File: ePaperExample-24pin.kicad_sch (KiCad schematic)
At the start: 21 parts, among them J1 Conn_01x24_MountingPin, Q1 Q_NMOS_GSD

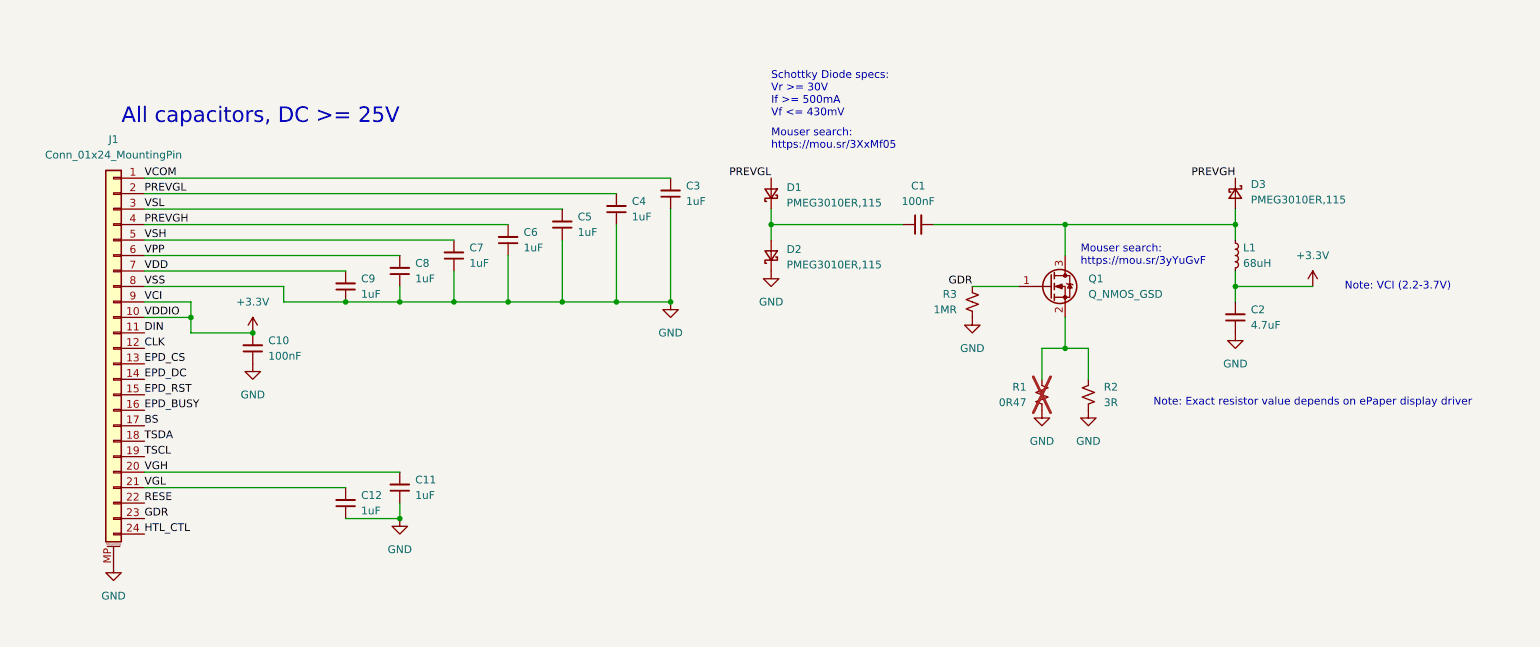
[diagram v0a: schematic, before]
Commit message: Updated to reflect tested board
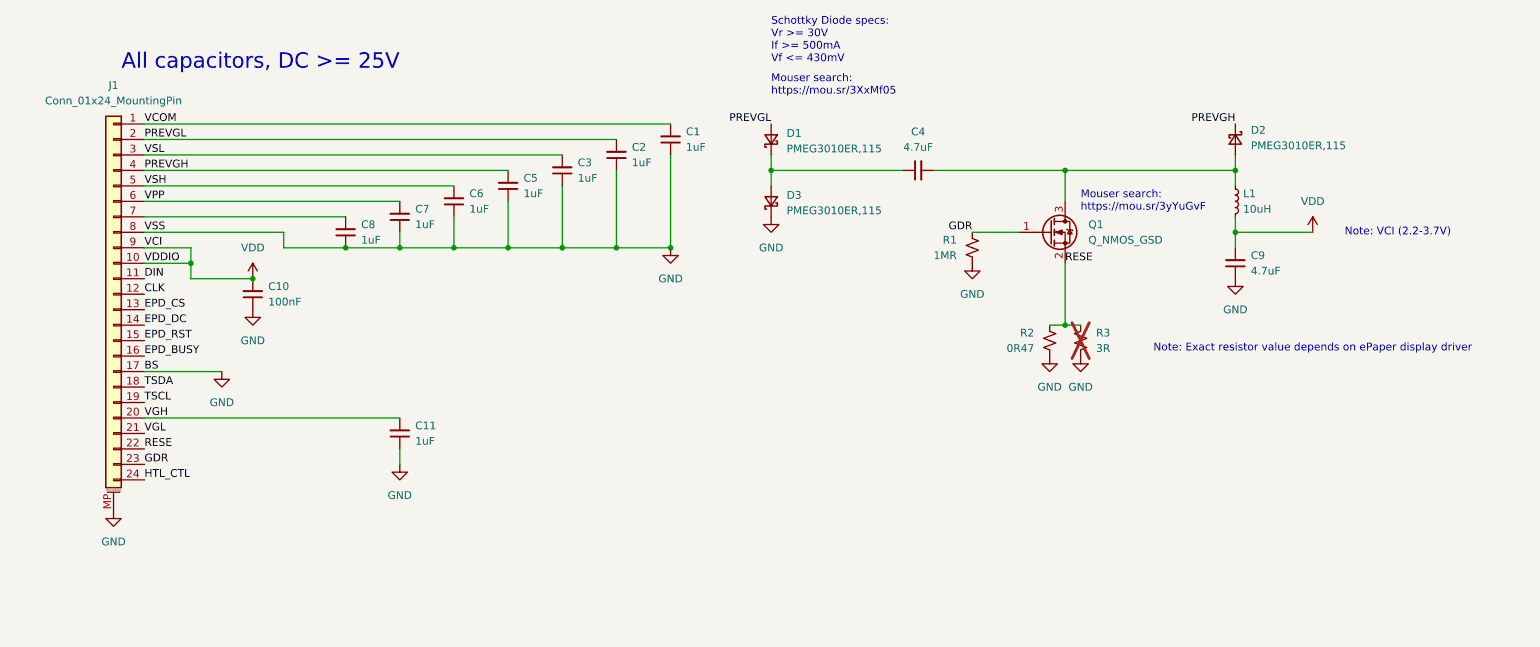
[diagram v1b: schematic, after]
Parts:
- removed C12: 1uF, Capacitor_SMD:C_0402_1005Metric, symbol Device:C_Small
- C1: value 100nF -> 1uF; LCSC (none) -> C52923
- C10: LCSC (none) -> C307331
- C11, C3, C5, C6, C7, C8: LCSC (none) -> C52923
- C2: value 4.7uF -> 1uF; LCSC (none) -> C52923
- C4, C9: value 1uF -> 4.7uF; LCSC (none) -> C2858031
- D1, D2, D3: LCSC (none) -> C456106
- J1: LCSC (none) -> C2911766
- L1: value 68uH -> 10uH; footprint Inductor_SMD:L_Bourns-SRN6028 -> Inductor_SMD:L_0805_2012Metric; LCSC (none) -> C2909263; MPN NR6028T680M -> (none)
- Q1: LCSC (none) -> C414015
- R1: value 0R47 -> 1MR; footprint (none) -> Resistor_SMD:R_0402_1005Metric; LCSC (none) -> C26083; now fitted; now in the parts list
- R2: value 3R -> 0R47; LCSC (none) -> C186564
- R3: value 1MR -> 3R; footprint Resistor_SMD:R_0402_1005Metric -> Resistor_SMD:R_0603_1608Metric; LCSC (none) -> C23157; now not fitted
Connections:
- net BS is gone; now on net GND: J1.17 (Pin_17)
- net GDR: now also R1.1; no longer R3.1
- net GND: now also C1.1, D3.1 (K); no longer C4.1, D2.1 (K)
- net PREVGH: now also C5.2, D2.1 (K); no longer C6.2, D3.1 (K)
- net PREVGL: now also C2.2; no longer C4.2
- net RESE: now also Q1.2 (S), R2.1, R3.1
- net VCOM: now also C1.2; no longer C3.2
- net VDD: now also C10.2, J1.10 (Pin_10), J1.9 (Pin_9), L1.2; no longer J1.7 (Pin_7)
- net VPP: now also C7.2; no longer C8.2
- net VSH: now also C6.2; no longer C7.2
- net VSL: now also C3.2; no longer C5.2
- net at L1.1, Q1.3 (D): now also C4.2, D2.2 (A); no longer C1.2, D3.2 (A)
- removed net +3.3V: C10.2, C2.2, J1.10 (Pin_10), J1.9 (Pin_9), L1.2
- new net: C4.1, D1.1 (K), D3.2 (A)
- new net: C8.2, J1.7 (Pin_7)

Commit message: Added updated schematic, added PCB layout
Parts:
- added C12: 1uF, Capacitor_SMD:C_0402_1005Metric, symbol Device:C_Small
- added J2: Conn_01x08_Socket, Connector_PinHeader_2.54mm:PinHeader_1x08_P2.54mm_Vertical, symbol Connector:Conn_01x08_Socket
- added SW1: SW_SPDT, Button_Switch_SMD:SW_SPDT_PCM12, symbol Switch:SW_SPDT
- R3: now fitted
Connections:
- net CLK: now also J2.3 (Pin_3)
- net DIN: now also J2.2 (Pin_2)
- net EPD_BUSY: now also J2.7 (Pin_7)
- net EPD_CS: now also J2.4 (Pin_4)
- net EPD_DC: now also J2.5 (Pin_5)
- net EPD_RST: now also J2.6 (Pin_6)
- net GND: now also C12.1, J2.8 (Pin_8)
- net RESE: now also SW1.2 (B); no longer R2.1, R3.1
- net VDD: now also J2.1 (Pin_1)
- net VGL: now also C12.2
- new net: R2.1, SW1.3 (C)
- new net: R3.1, SW1.1 (A)
